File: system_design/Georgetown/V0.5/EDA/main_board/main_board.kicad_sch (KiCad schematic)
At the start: 23 parts, among them U1 top_rail_v2, U2 DS3231M, U3 INA219AxD, U5 KA78M05_TO252

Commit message: PCB modified
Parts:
- removed F1: Fuse, Resistor_SMD:R_0603_1608Metric_Pad1.05x0.95mm_HandSolder, symbol Device:Fuse
- removed Micro_SD1: small_microSD, ARTS-Lab:small_microSD_v2, symbol main_board-rescue:small_microSD-whs5-rescue
- removed Power_IN1: XP60PW, ARTS-Lab:XT60PW, symbol main_board-rescue:XP60PW-whs5-rescue-whs5-rescue
- removed U1: top_rail_v2, ARTS-Lab:top_rail_v2, symbol main_board-rescue:top_rail_v2-ARTS-Lab
- removed switch1: grounded_switch, ARTS-Lab:grounded_switch, symbol main_board-rescue:grounded_switch-whs5-rescue-whs5-rescue
- added J1: B3B-XH-A_LF__SN_, XH2.54:XH2.54, symbol XH2.54:B3B-XH-A_LF__SN_
- added P1: SD card socket, ST-TF-003A:SUNTECH_ST-TF-003A, symbol ST-TF-003A:ST-TF-003A
- added U1: HX-2S-JH10, megasaturnv_custom_components:HX-2S-JH10, symbol megasaturnv_custom_components:HX-2S-JH10
- added U4: BME280_module, megasaturnv_custom_components:BME280_module, symbol megasaturnv_custom_components:BME280_module
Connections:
- net GND: now also P1.6 (VSS), P1.G1 (GND), P1.G2 (GND), P1.G3 (GND), P1.G4 (GND), U1.1 (P-)
- net at A1.17 (3V3), C1.1, R3.1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: now also P1.4 (VDD)
- net at A1.15 (D12), nRF24L01+1.8 (MISO): now also P1.7 (DAT0/MISO)
- net at D1.1 (K): now also C2.1, R2.1, U3.8 (IN+)
- net at D1.2 (A): now also U1.2 (P+)

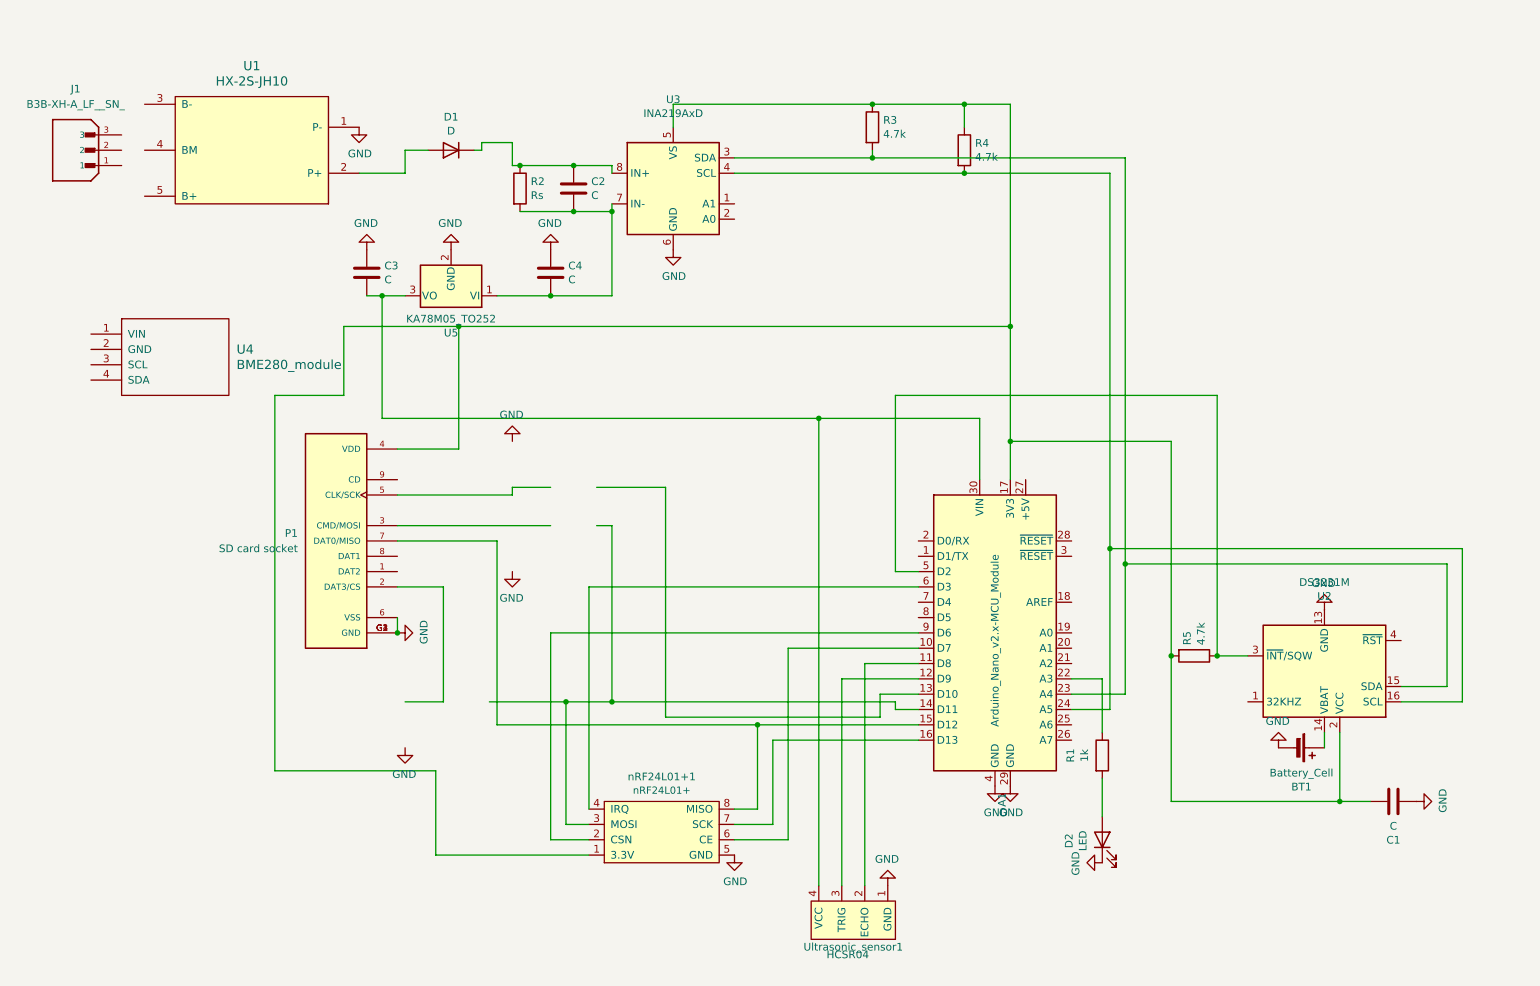
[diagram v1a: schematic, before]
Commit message: CAD updated
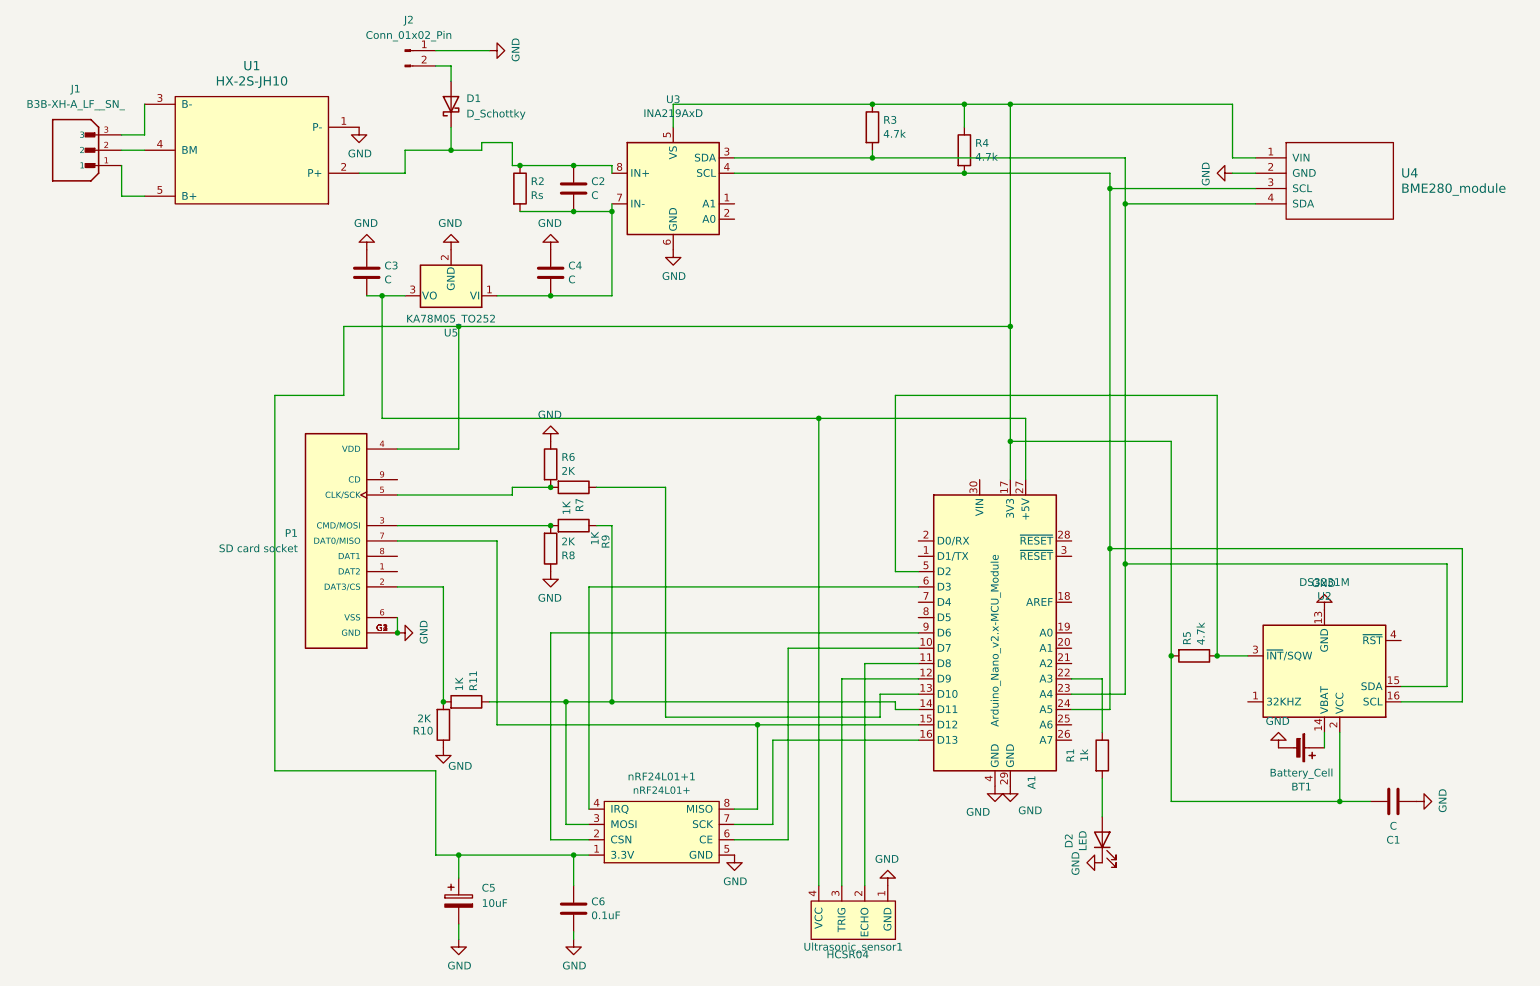
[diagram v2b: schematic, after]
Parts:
- removed D1: D, Diode_SMD:D_1206_3216Metric_Pad1.42x1.75mm_HandSolder, symbol Device:D
- added C5: 10uF, Capacitor_THT:CP_Radial_D4.0mm_P2.00mm, symbol Device:C_Polarized
- added C6: 0.1uF, Capacitor_SMD:C_1206_3216Metric_Pad1.33x1.80mm_HandSolder, symbol Device:C
- added D1: D_Schottky, Diode_SMD:D_1206_3216Metric_Pad1.42x1.75mm_HandSolder, symbol Device:D_Schottky
- added J2: Conn_01x02_Pin, Connector_PinHeader_2.54mm:PinHeader_1x02_P2.54mm_Vertical, symbol Connector:Conn_01x02_Pin
- added R10, R6, R8: 2K, Capacitor_SMD:C_1206_3216Metric_Pad1.33x1.80mm_HandSolder, symbol Device:R
- added R11, R7, R9: 1K, Capacitor_SMD:C_1206_3216Metric_Pad1.33x1.80mm_HandSolder, symbol Device:R
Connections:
- net GND: now also U4.2 (GND), C5.2, C6.2, J2.1 (Pin_1), R10.1, R6.1, R8.1
- net at A1.17 (3V3), C1.1, P1.4 (VDD)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: now also U4.1 (VIN), C5.1, C6.1
- net at A1.14 (D11), nRF24L01+1.3 (MOSI): now also R11.1, R9.1
- net at C3.2, U5.3 (VO), Ultrasonic_sensor1.4 (VCC): now also A1.27 (+5V); no longer A1.30 (VIN)
- net at A1.23 (A4), R3.2, U2.15 (SDA)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: now also U4.4 (SDA)
- net at A1.24 (A5), R4.2, U2.16 (SCL)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: now also U4.3 (SCL)
- net at C2.1, R2.1, U3.8 (IN+): now also U1.2 (P+), D1.1 (K)
- net at A1.13 (D10): now also R7.1
- net at U1.3 (B-): now also J1.3
- net at U1.4 (BM): now also J1.2
- net at U1.5 (B+): now also J1.1
- net at P1.2 (DAT3/CS): now also R10.2, R11.2
- net at P1.3 (CMD/MOSI): now also R8.2, R9.2
- net at P1.5 (CLK/SCK): now also R6.2, R7.2
- new net: D1.2 (A), J2.2 (Pin_2)
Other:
- moved on the sheet: U4

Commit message: PCB design modified
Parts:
- added SW1: SW_Wuerth_450301014042, Button_Switch_THT:SW_Slide-03_Wuerth-WS-SLTV_10x2.5x6.4_P2.54mm, symbol Switch:SW_Wuerth_450301014042
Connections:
- net at C2.1, R2.1, U3.8 (IN+): now also SW1.1 (B); no longer D1.1 (K), U1.2 (P+)
- new net: D1.1 (K), SW1.2 (C), U1.2 (P+)
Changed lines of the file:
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@@
 	(wire
 		(pts
-			(xy 95.25 34.29) (xy 95.25 38.1)
-		)
-		(stroke
-			(width 0)
-			(type default)
-		)
-	)
-	(wire
-		(pts
 			(xy 132.08 144.78) (xy 135.89 144.78)
 		)
@@
 	(wire
 		(pts
-			(xy 85.09 35.56) (xy 90.17 35.56)
-		)
-		(stroke
-			(width 0)
-			(type default)
-		)
-	)
-	(wire
-		(pts
 			(xy 101.6 115.57) (xy 162.56 115.57)
 		)
@@
 	(wire
 		(pts
-			(xy 90.17 35.56) (xy 90.17 34.29)
-		)
-		(stroke
-			(width 0)
-			(type default)
-		)
-	)
-	(wire
-		(pts
 			(xy 86.36 152.4) (xy 86.36 156.21)
 		)
@@
 	(wire
 		(pts
-			(xy 90.17 34.29) (xy 95.25 34.29)
-		)
-		(stroke
-			(width 0)
-			(type default)
-		)
-	)
-	(wire
-		(pts
 			(xy 101.6 59.69) (xy 111.76 59.69)
 		)
@@
 					(unit 1)
 				)
+			)
+		)
+	)
+	(symbol
+		(lib_id "Switch:SW_Wuerth_450301014042")
+		(at 90.17 38.1 180)
+		(unit 1)
+		(exclude_from_sim no)
+		(in_bom yes)
+		(on_board yes)
+		(dnp no)
+		(property "Reference" "SW1"
+			(at 84.074 37.846 0)
+			(effects
+				(font
+					(size 1.27 1.27)
+				)
+			)
+		)
+		(property "Value" "SW_Wuerth_450301014042"
+			(at 82.296 43.434 0)
+			(effects
+				(font
+					(size 1.27 1.27)
+				)
+			)
+		)
+		(property "Footprint" "Button_Switch_THT:SW_Slide-03_Wuerth-WS-SLTV_10x2.5x6.4_P2.54mm"
+			(at 90.17 27.94 0)
+			(effects
+				(font
+					(size 1.27 1.27)
+				)
+				(hide yes)
+			)
+		)
+		(property "Datasheet" "https://www.we-online.com/components/products/datasheet/450301014042.pdf"
+			(at 90.17 30.48 0)
+			(effects
+				(font
+					(size 1.27 1.27)
+				)
+				(hide yes)
+			)
+		)
+		(property "Description" "Switch slide, single pole double throw"
+			(at 90.17 38.1 0)
+			(effects
+				(font
+					(size 1.27 1.27)
+				)
+				(hide yes)
+			)
+		)
+		(pin "3"
+		)
+		(pin "1"
+		)
+		(pin "2"
+		)
+		(instances
+			(project ""
+				(path "/6055025c-91fc-4d42-99c1-24bcdc7ae09f"
+					(reference "SW1")
+					(unit 1)
+				)

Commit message: PCB design changed
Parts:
- D1: footprint Diode_SMD:D_1206_3216Metric_Pad1.42x1.75mm_HandSolder -> Diode_SMD:D_1206_3216Metric
